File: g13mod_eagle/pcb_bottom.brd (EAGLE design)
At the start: 96.4 x 39.8 mm, 0 parts

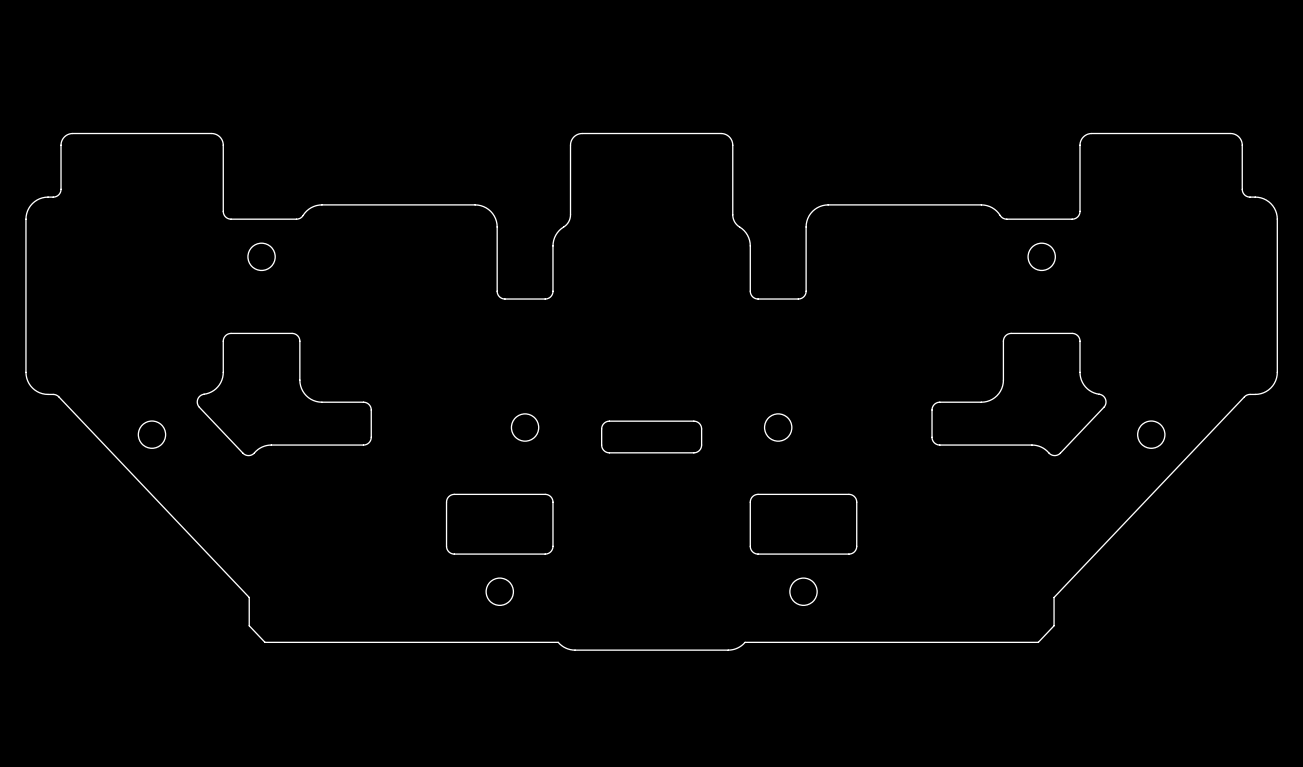
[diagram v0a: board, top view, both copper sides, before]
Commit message: Add switches
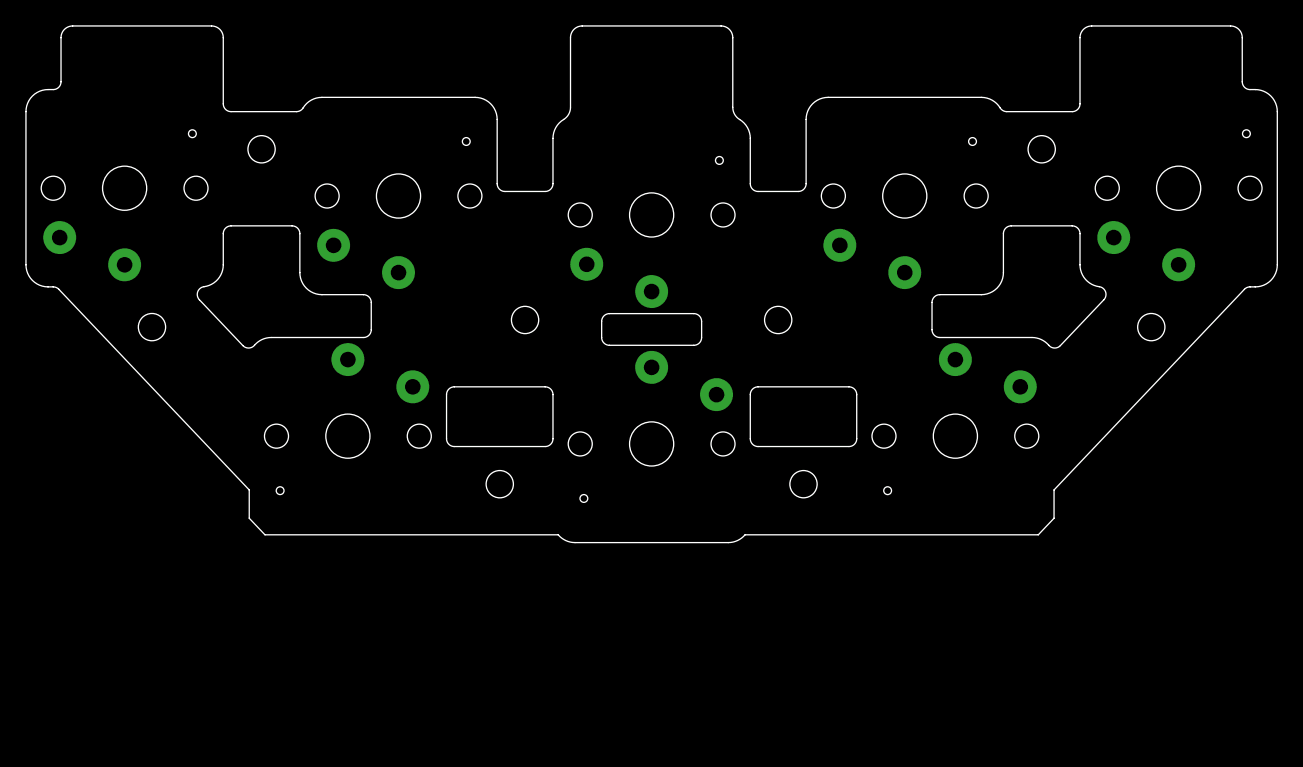
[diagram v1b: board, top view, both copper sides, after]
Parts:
- added U$1, U$2, U$3, U$4, U$5, U$6, U$7, U$8: KEYSWITCH-PLAIN-CHOC-1U, Keyboard:CHOC-1U
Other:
- outline, holes or cut-outs redrawn

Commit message: wiring bottom pcb
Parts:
- added JP1, JP2: (no value), pinhead-half-pitch:THROUHOLE09
- added LED1: B38G3RGB, led_rgb:B38G3RGB
- added R1, R2, R3: (no value), rcl:R0603
- renumbered U$1 to G15, U$2 to G16, U$3 to G17, U$4 to G18, U$5 to G19, U$6 to G20, U$7 to G21, U$8 to G22
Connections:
- new net B: JP1.9, R2.1
- new net CN6_11: G20.CHOC2, JP1.1
- new net CN6_13: G22.CHOC2, JP1.2
- new net CN6_14: G21.CHOC2, JP1.3
- new net CN6_17: G17.CHOC2, JP1.4
- new net CN6_18: G15.CHOC1, G16.CHOC1, JP1.5
- new net CN6_8: G18.CHOC2, JP2.8
- new net CN6_9: G19.CHOC2, JP2.9
- new net CN7_13: G19.CHOC1, JP2.5
- new net CN7_14: G18.CHOC1, JP2.6
- new net CN7_15: G17.CHOC1, JP2.7
- new net CN7_4: G15.CHOC2, JP2.1
- new net CN7_6: G22.CHOC1, JP2.2
- new net CN7_7: G20.CHOC1, G21.CHOC1, JP2.3
- new net CN7_8: G16.CHOC2, JP2.4
- new net G: JP1.7, R1.1
- new net N$1: LED1.1, R1.2
- new net N$2: LED1.2, R2.2
- new net N$3: LED1.4, R3.2
- new net R: JP1.8, R3.1
- new net V: JP1.6, LED1.3

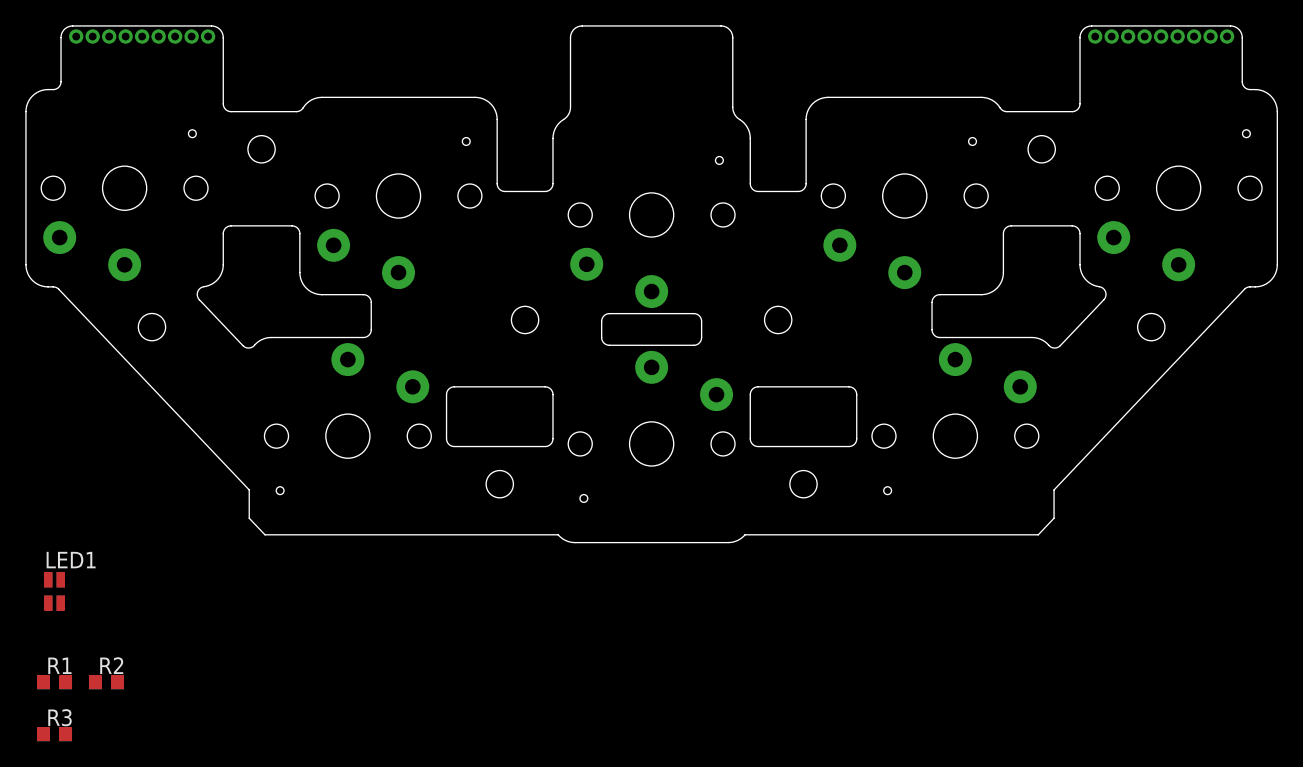
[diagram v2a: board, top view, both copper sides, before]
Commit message: wiring bottom pcb
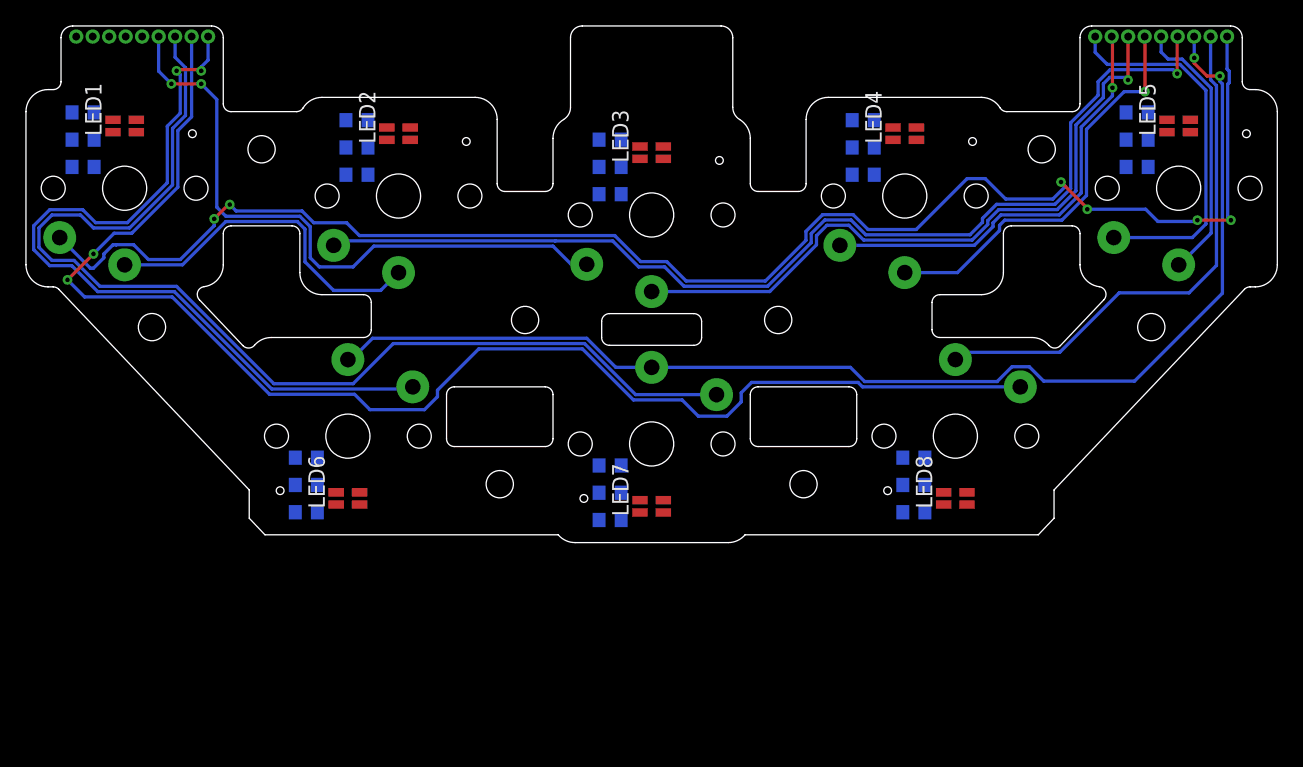
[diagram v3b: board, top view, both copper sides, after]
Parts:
- added LED2, LED3, LED4, LED5, LED6, LED7, LED8: B38G3RGB, led_rgb:B38G3RGB
- added R10, R11, R12, R13, R14, R15, R16, R17, R18, R19, R20, R21, R22, R23, R24, R4, R5, R6, R7, R8, R9: (no value), rcl:R0603
- moved R2 43.9 mm to (-43.8, 7.90), flipped to the bottom, turned to 180 degrees
- moved R3 43.8 mm to (-43.8, 3.70), flipped to the bottom, turned to 180 degrees
- moved R1 41.9 mm to (-43.8, 5.80), flipped to the bottom, turned to 180 degrees
- moved LED1 36.3 mm to (-40.6, 6.86), turned to 90 degrees
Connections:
- new net N$10: LED4.1, R10.2
- new net N$11: LED4.2, R11.2
- new net N$12: LED4.4, R12.2
- new net N$13: LED5.1, R13.2
- new net N$14: LED5.2, R14.2
- new net N$15: LED5.4, R15.2
- new net N$16: LED6.1, R16.2
- new net N$17: LED6.2, R17.2
- new net N$18: LED6.4, R18.2
- new net N$19: LED7.1, R19.2
- new net N$20: LED7.2, R20.2
- new net N$21: LED7.4, R21.2
- new net N$22: LED8.1, R22.2
- new net N$23: LED8.2, R23.2
- new net N$24: LED8.4, R24.2
- new net N$4: LED2.1, R4.2
- new net N$5: LED2.2, R5.2
- new net N$6: LED2.4, R6.2
- new net N$7: LED3.1, R7.2
- new net N$8: LED3.2, R8.2
- new net N$9: LED3.4, R9.2
- net B: now also R11.1, R14.1, R17.1, R20.1, R23.1, R5.1, R8.1
- net G: now also R10.1, R13.1, R16.1, R19.1, R22.1, R4.1, R7.1
- net R: now also R12.1, R15.1, R18.1, R21.1, R24.1, R6.1, R9.1
- net V: now also LED2.3, LED3.3, LED4.3, LED5.3, LED6.3, LED7.3, LED8.3
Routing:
- net CN7_4: track 0.00 -> 119.3 mm, vias 0 -> 6
- net CN6_13: track 0.00 -> 107.1 mm, vias 0 -> 2
- net CN7_7: track 0.00 -> 94.4 mm, vias 0 -> 2
- net CN6_14: track 0.00 -> 85.6 mm
- net CN7_8: track 0.00 -> 81.6 mm, vias 0 -> 1
- net CN6_11: track 0.00 -> 62.1 mm, vias 0 -> 2
- net CN7_15: track 0.00 -> 52.1 mm, vias 0 -> 1
- net CN6_17: track 0.00 -> 49.4 mm, vias 0 -> 2
- net CN7_6: track 0.00 -> 40.9 mm
- net CN6_8: track 0.00 -> 33.5 mm, vias 0 -> 1
- net CN7_14: track 0.00 -> 31.8 mm, vias 0 -> 1
- net CN6_9: track 0.00 -> 28.8 mm
- net CN6_18: track 0.00 -> 26.7 mm
- net CN7_13: track 0.00 -> 20.9 mm

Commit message: wiring bottom pcb
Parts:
- turned R24 to 180 degrees
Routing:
- net B: track 0.00 -> 212.7 mm, vias 0 -> 9
- net V: track 0.00 -> 211.4 mm, vias 0 -> 4
- net G: track 0.00 -> 206.2 mm, vias 0 -> 13
- net R: track 0.00 -> 195.3 mm, vias 0 -> 8
- net CN6_18: track 26.7 -> 45.8 mm, vias 0 -> 1
- net N$24: track 0.00 -> 4.92 mm, vias 0 -> 1
- net N$9: track 0.00 -> 4.92 mm, vias 0 -> 1
- net N$6: track 0.00 -> 4.88 mm, vias 0 -> 1
- net N$15: track 0.00 -> 4.88 mm, vias 0 -> 1
- net N$12: track 0.00 -> 4.88 mm, vias 0 -> 1
- net N$3: track 0.00 -> 4.88 mm, vias 0 -> 1
- net N$18: track 0.00 -> 4.85 mm, vias 0 -> 1
- net N$21: track 0.00 -> 4.84 mm, vias 0 -> 1
- net N$19: track 0.00 -> 3.94 mm, vias 0 -> 1
- net N$22: track 0.00 -> 3.89 mm, vias 0 -> 1
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
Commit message: Edit width
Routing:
- net V: track 211.4 -> 230.9 mm, vias 4 -> 3
- net B: track 212.7 -> 211.5 mm

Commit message: Fix bug
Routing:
- net G: track 205.7 -> 204.6 mm
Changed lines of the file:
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@@
 <wire x1="-36.2" y1="-1.4700125" x2="-32.4275" y2="2.3024875" width="0.254" layer="1"/>
 <wire x1="-32.4275" y1="2.3024875" x2="-32.4275" y2="5.6275" width="0.254" layer="1"/>
-<wire x1="-27.3" y1="-17.5" x2="-24.7" y2="-14.9" width="0.254" layer="16"/>
-<wire x1="-24.7" y1="-14.9" x2="-22.6" y2="-14.9" width="0.254" layer="16"/>
-<wire x1="-22.6" y1="-14.9" x2="-21.373" y2="-16.127" width="0.254" layer="16"/>
-<wire x1="-21.373" y1="-16.127" x2="-21.373" y2="-22.6395" width="0.254" layer="16"/>
+<wire x1="-27.3" y1="-17.5" x2="-24.5" y2="-14.7" width="0.254" layer="16"/>
+<wire x1="-24.5" y1="-14.7" x2="-22.4" y2="-14.7" width="0.254" layer="16"/>
+<wire x1="-22.4" y1="-14.7" x2="-21.073" y2="-16.027" width="0.254" layer="16"/>
+<wire x1="-21.073" y1="-16.027" x2="-21.073" y2="-22.9395" width="0.254" layer="16"/>
 <wire x1="-9.9" y1="-23.9" x2="-5.3" y2="-19.3" width="0.254" layer="16"/>
 <wire x1="-5.3" y1="-19.3" x2="-4.05" y2="-19.3" width="0.254" layer="16"/>
-<wire x1="-21.373" y1="-22.6395" x2="-20.1125" y2="-23.9" width="0.254" layer="16"/>
+<wire x1="-21.073" y1="-22.9395" x2="-20.1125" y2="-23.9" width="0.254" layer="16"/>
 <wire x1="-20.1125" y1="-23.9" x2="-9.9" y2="-23.9" width="0.254" layer="16"/>
 <wire x1="19.35" y1="-18.7" x2="19" y2="-19.05" width="0.254" layer="16"/>
@@
 <wire x1="28.2" y1="2.8" x2="26.8" y2="4.2" width="0.254" layer="1"/>
 <wire x1="26.8" y1="4.2" x2="15.3" y2="4.2" width="0.254" layer="1"/>
-<wire x1="-28.5" y1="-15.3" x2="-28.5" y2="-15.5" width="0.254" layer="1"/>
-<via x="-28.5" y="-15.5" extent="1-16" drill="0.35"/>
-<wire x1="-28.5" y1="-15.5" x2="-29.5" y2="-15.5" width="0.254" layer="16"/>
+<wire x1="-29.2" y1="-14.6" x2="-29.2" y2="-15.4" width="0.254" layer="1"/>
+<via x="-29.2" y="-15.4" extent="1-16" drill="0.35"/>
+<wire x1="-29.2" y1="-15.4" x2="-29.4" y2="-15.4" width="0.254" layer="16"/>
 <wire x1="-30.152" y1="-16.152" x2="-30.152" y2="-18.698" width="0.254" layer="16"/>
 <wire x1="-30.152" y1="-18.698" x2="-28.625" y2="-20.225" width="0.254" layer="16"/>
-<wire x1="-36.6064" y1="-7.1936" x2="-28.5" y2="-15.3" width="0.254" layer="1"/>
-<wire x1="-29.5" y1="-15.5" x2="-30.152" y2="-16.152" width="0.254" layer="16"/>
+<wire x1="-36.6064" y1="-7.1936" x2="-29.2" y2="-14.6" width="0.254" layer="1"/>
+<wire x1="-29.4" y1="-15.4" x2="-30.152" y2="-16.152" width="0.254" layer="16"/>
 <wire x1="-33.5" y1="5.4" x2="-33.2339" y2="5.4" width="0.254" layer="1"/>
 <wire x1="-33.2339" y1="5.4" x2="-32.8339" y2="5" width="0.254" layer="1"/>
@@
 <wire x1="41.5" y1="7.335" x2="41.5" y2="8.2" width="0.254" layer="1"/>
 <wire x1="34.2" y1="9" x2="33.1" y2="7.9" width="0.254" layer="1"/>
-<wire x1="33" y1="7.8" x2="33.1" y2="7.9" width="0.254" layer="1"/>
 <wire x1="33.1" y1="7.9" x2="33.05636875" y2="7.9" width="0.254" layer="1"/>
 <wire x1="33.05636875" y1="7.9" x2="32.78886875" y2="7.6325" width="0.254" layer="1"/>
@@
 <wire x1="-16.5" y1="-13.5" x2="-16.5" y2="-14" width="0.254" layer="16"/>
 <wire x1="-16.5" y1="-14" x2="-17.5" y2="-15" width="0.254" layer="16"/>
-<wire x1="-21.7" y1="-15" x2="-22.8872" y2="-13.8128" width="0.254" layer="16"/>
+<wire x1="-19.7" y1="-15" x2="-20.8872" y2="-13.8128" width="0.254" layer="16"/>
 <wire x1="-42.8872" y1="-6.3128" x2="-44.4" y2="-4.8" width="0.254" layer="16"/>
 <wire x1="-44.4" y1="-4.8" x2="-44.9" y2="-4.8" width="0.254" layer="16"/>
@@
 <wire x1="-1.403075" y1="-14.2464" x2="-5.336675" y2="-10.3128" width="0.254" layer="16"/>
 <wire x1="-5.336675" y1="-10.3128" x2="-13.3128" y2="-10.3128" width="0.254" layer="16"/>
-<wire x1="-17.5" y1="-15" x2="-21.7" y2="-15" width="0.254" layer="16"/>
-<wire x1="-22.8872" y1="-13.8128" x2="-29.436675" y2="-13.8128" width="0.254" layer="16"/>
+<wire x1="-17.5" y1="-15" x2="-19.7" y2="-15" width="0.254" layer="16"/>
+<wire x1="-20.8872" y1="-13.8128" x2="-29.436675" y2="-13.8128" width="0.254" layer="16"/>
 <wire x1="-29.436675" y1="-13.8128" x2="-36.936675" y2="-6.3128" width="0.254" layer="16"/>
 <wire x1="-36.936675" y1="-6.3128" x2="-42.8872" y2="-6.3128" width="0.254" layer="16"/>
@@
 <wire x1="32.7300875" y1="-0.257075" x2="30.83650625" y2="1.63650625" width="0.254" layer="1"/>
 <via x="32.757075" y="-0.257075" extent="1-16" drill="0.35"/>
-<wire x1="32.757075" y1="-0.257075" x2="38.757075" y2="-0.257075" width="0.254" layer="16"/>
-<wire x1="38.757075" y1="-0.257075" x2="39" y2="-0.5" width="0.254" layer="16"/>
+<wire x1="38.657075" y1="-0.157075" x2="32.857075" y2="-0.157075" width="0.254" layer="16"/>
+<wire x1="32.757075" y1="-0.257075" x2="32.857075" y2="-0.157075" width="0.254" layer="16"/>
+<wire x1="38.657075" y1="-0.157075" x2="39" y2="-0.5" width="0.254" layer="16"/>
 <wire x1="39" y1="-0.5" x2="41.9424" y2="-0.5" width="0.254" layer="16"/>
 <wire x1="41.9424" y1="-0.5" x2="42.0424" y2="-0.4" width="0.254" layer="16"/>
@@
 <via x="-20.4" y="4.9" extent="1-16" drill="0.35"/>
 <wire x1="-20.4" y1="4.9" x2="-20.4" y2="5.785" width="0.254" layer="1"/>
-<wire x1="-20.4" y1="4.9" x2="-20.3936" y2="4.9" width="0.254" layer="16"/>
 </signal>
 <signal name="N$5">

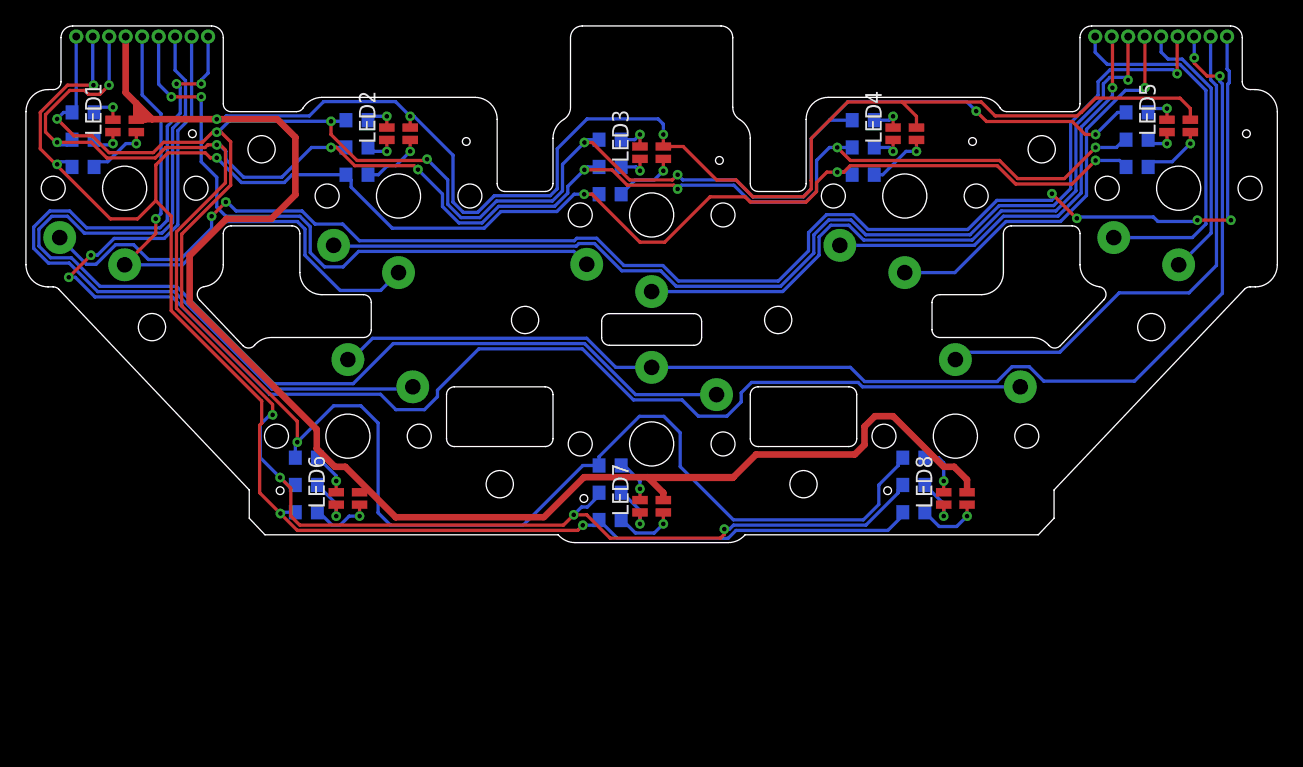
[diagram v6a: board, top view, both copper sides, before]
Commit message: Fix LED color
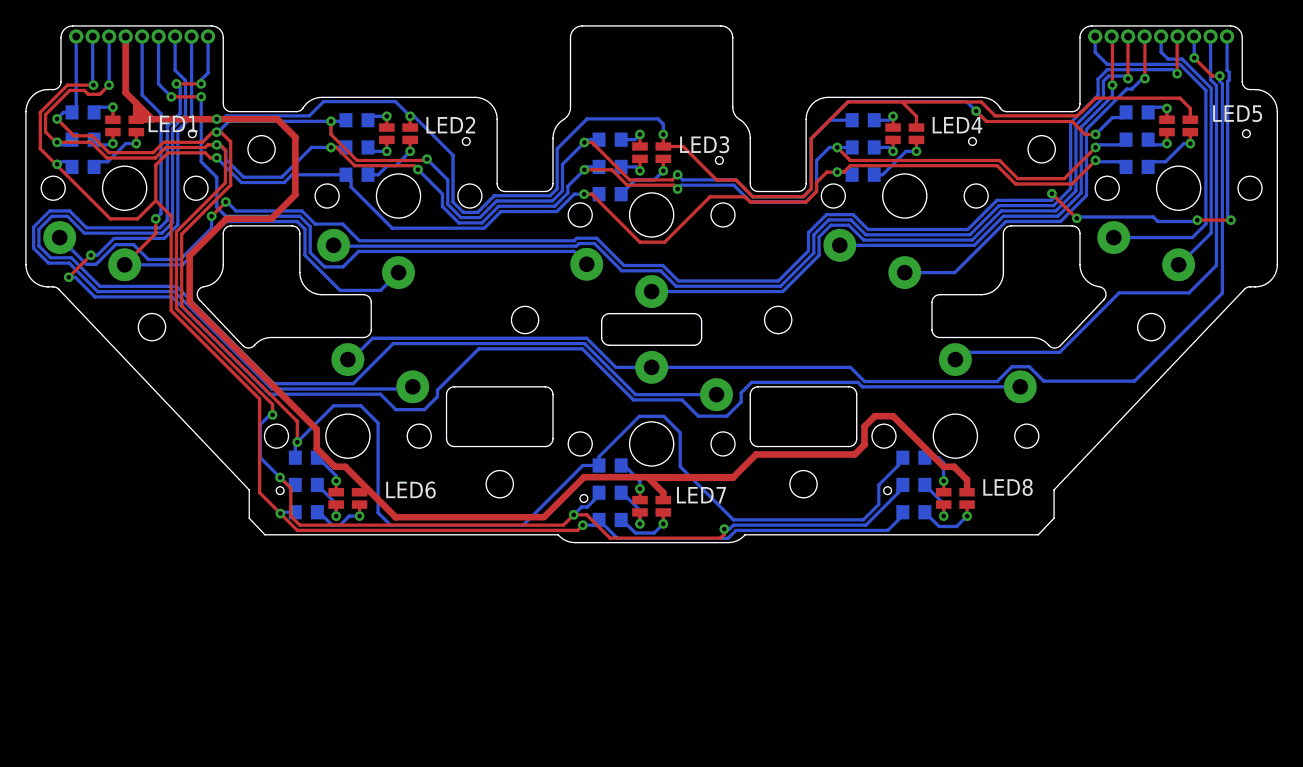
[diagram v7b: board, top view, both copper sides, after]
